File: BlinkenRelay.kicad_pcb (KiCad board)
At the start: 2 copper layers, 90 x 62 mm, 23 parts, among them J1 Conn_02x07_Odd_Even, J2 Conn_01x08_Pin, J3 Conn_01x08_Socket, SW1 SW_DIP_x01, U1 LTV-817, U2 LTV-817, U3 LTV-817, U4 LTV-817, U5 LTV-817, U6 LTV-817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

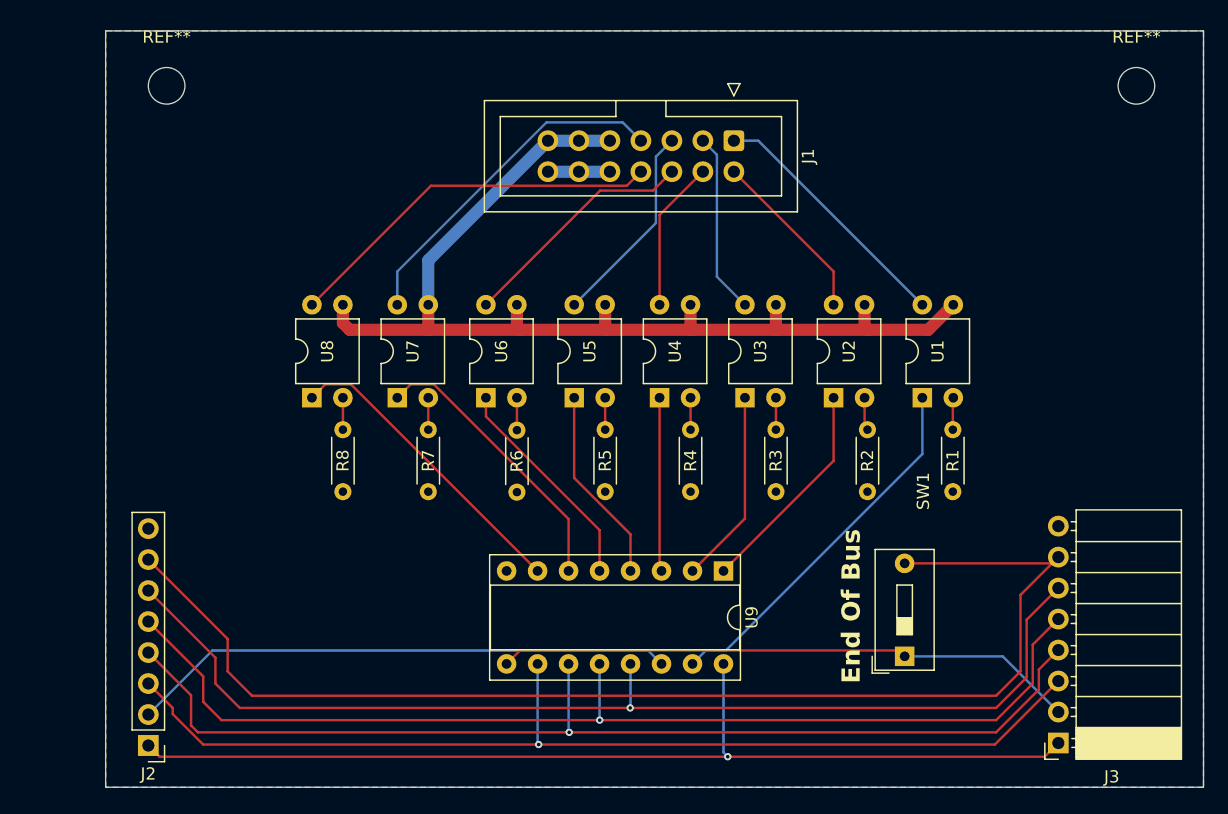
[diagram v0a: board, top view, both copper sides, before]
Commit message: New revision. Fixed switched Pins.
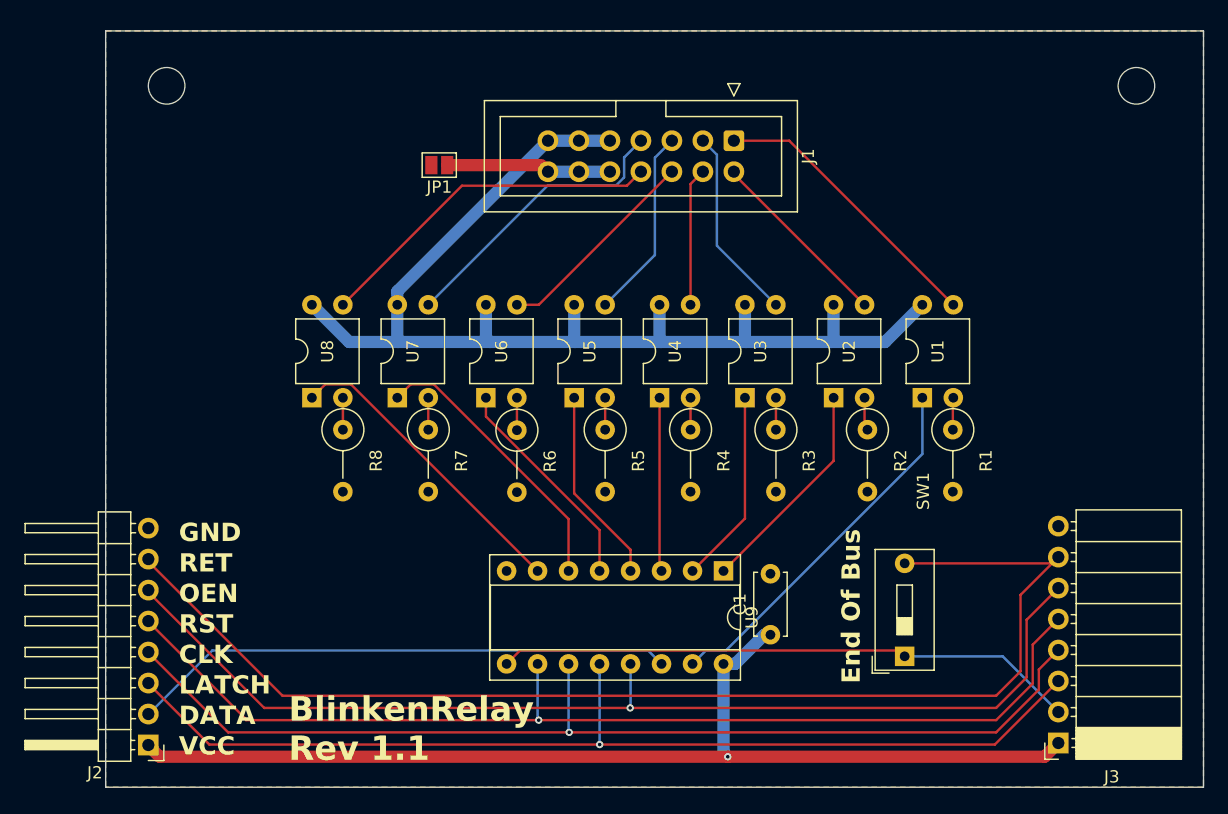
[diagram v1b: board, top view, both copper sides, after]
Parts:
- added C1: 10n, Capacitor_THT:C_Disc_D5.0mm_W2.5mm_P5.00mm, F.Cu at (148.5, 74.5)
- added JP1: Jumper_2_Open, Jumper:SolderJumper-2_P1.3mm_Open_Pad1.0x1.5mm, F.Cu at (121.3, 36.0)
- J2: footprint Connector_PinHeader_2.54mm:PinHeader_1x08_P2.54mm_Vertical -> Connector_PinHeader_2.54mm:PinHeader_1x08_P2.54mm_Horizontal
- R1, R2, R3, R4, R5, R6, R7, R8: value 180 -> 510; footprint Resistor_THT:R_Axial_DIN0204_L3.6mm_D1.6mm_P5.08mm_Horizontal -> Resistor_THT:R_Axial_DIN0309_L9.0mm_D3.2mm_P5.08mm_Vertical
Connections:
- U1 pad 3: +24V -> Kanal 1
- U1 pad 4: Kanal 1 -> +24V
- U2 pad 3: +24V -> Kanal 2
- U2 pad 4: Kanal 2 -> +24V
- U3 pad 3: +24V -> Kanal 3
- U3 pad 4: Kanal 3 -> +24V
- U4 pad 3: +24V -> Kanal 4
- U4 pad 4: Kanal 4 -> +24V
- U5 pad 3: +24V -> Kanal 5
- U5 pad 4: Kanal 5 -> +24V
- U6 pad 3: +24V -> Kanal 6
- U6 pad 4: Kanal 6 -> +24V
- U7 pad 3: +24V -> Kanal 7
- U7 pad 4: Kanal 7 -> +24V
- U8 pad 3: +24V -> Kanal 8
- U8 pad 4: Kanal 8 -> +24V
- U9 pad 10: Strobe -> Reset
- U9 pad 12: Reset -> Strobe
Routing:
- net Net-(J1-Pin_10): track 5.08 -> 13.6 mm
- net +24V: track 87.8 -> 94.9 mm
- net VCC: track 83.2 -> 88.0 mm
- net Kanal 7: track 28.4 -> 24.0 mm
- net Kanal 6: track 19.8 -> 17.2 mm
- net Kanal 1: track 21.0 -> 23.6 mm
- net Kanal 8: track 31.5 -> 28.9 mm
- net Return: track 102.0 -> 99.6 mm
- net Clock: track 88.1 -> 86.7 mm
- net Output Enable: track 90.3 -> 89.0 mm
- net Reset: track 89.1 -> 87.9 mm
- net Kanal 3: track 14.9 -> 15.9 mm
- net Kanal 5: track 16.8 -> 15.7 mm
- net Kanal 4: track 12.4 -> 11.3 mm
- net Kanal 2: track 14.3 -> 15.2 mm
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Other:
- board text added: "BlinkenRelay Rev 1.1"
- board text added: "CLK"
- board text added: "DATA"
- board text added: "GND"
- board text added: "LATCH"
- board text added: "OEN"
- board text added: "RET"
- board text added: "RST"
- board text added: "VCC"

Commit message: Added status LEDS and removed backups from git.
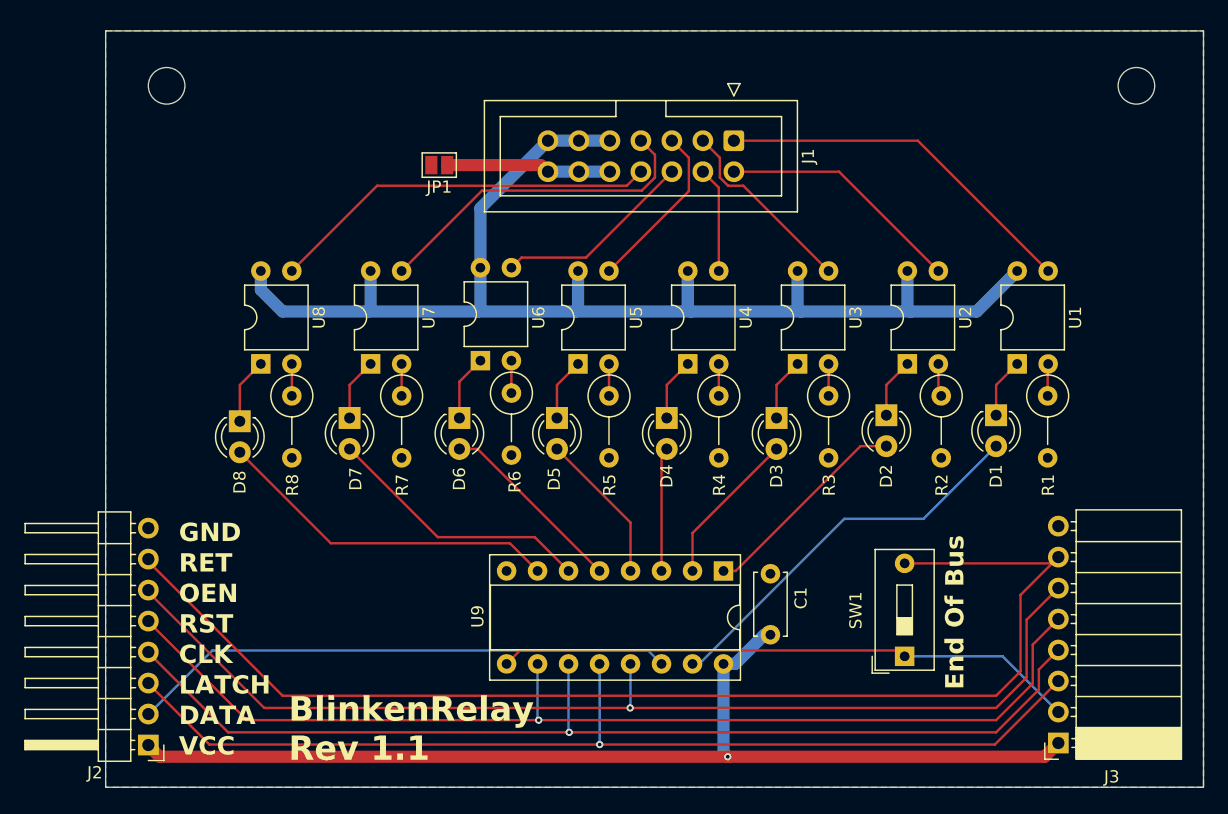
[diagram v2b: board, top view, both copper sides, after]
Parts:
- added D1: LED, LED_THT:LED_D3.0mm, F.Cu at (167.0, 56.5)
- added D2: LED, LED_THT:LED_D3.0mm, F.Cu at (158.0, 56.5)
- added D3: LED, LED_THT:LED_D3.0mm, F.Cu at (149.0, 56.7)
- added D4: LED, LED_THT:LED_D3.0mm, F.Cu at (140.0, 56.7)
- added D5: LED, LED_THT:LED_D3.0mm, F.Cu at (131.0, 56.7)
- added D6: LED, LED_THT:LED_D3.0mm, F.Cu at (123.0, 56.7)
- added D7: LED, LED_THT:LED_D3.0mm, F.Cu at (114.0, 56.7)
- added D8: LED, LED_THT:LED_D3.0mm, F.Cu at (105.0, 57.0)
- R1, R2, R3, R4, R5, R6, R7, R8: value 510 -> 140
- moved U1 8.25 mm to (168.7, 52.3)
- moved R1 8.25 mm to (171.2, 54.9)
- moved R2 6.65 mm to (162.5, 54.9)
- moved U2 6.65 mm to (159.7, 52.3)
- moved U3 5.13 mm to (150.7, 52.3)
- moved R3 5.13 mm to (153.3, 54.9)
- moved U8 5.02 mm to (106.7, 52.3)
- moved R8 5.02 mm to (109.3, 54.9)
- moved U4 3.61 mm to (141.7, 52.3)
- moved R4 3.61 mm to (144.3, 54.9)
- moved U7 3.53 mm to (115.7, 52.3)
- moved R7 3.53 mm to (118.3, 54.9)
- moved R6 3.07 mm to (127.3, 54.7)
- moved U6 3.07 mm to (124.7, 52.0)
- moved U5 2.79 mm to (132.7, 52.3)
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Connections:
- U1 pad 1: Net-(U9-QA) -> Net-(D1-K)
- U2 pad 1: Net-(U9-QB) -> Net-(D2-K)
- U3 pad 1: Net-(U9-QC) -> Net-(D3-K)
- U4 pad 1: Net-(U9-QD) -> Net-(D4-K)
- U5 pad 1: Net-(U9-QE) -> Net-(D5-K)
- U6 pad 1: Net-(U9-QF) -> Net-(D6-K)
- U7 pad 1: Net-(U9-QG) -> Net-(D7-K)
- U8 pad 1: Net-(U9-QH) -> Net-(D8-K)
- U9 pad 1: Net-(U9-QB) -> Net-(D2-A)
- U9 pad 15: Net-(U9-QA) -> Net-(D1-A)
- U9 pad 2: Net-(U9-QC) -> Net-(D3-A)
- U9 pad 3: Net-(U9-QD) -> Net-(D4-A)
- U9 pad 4: Net-(U9-QE) -> Net-(D5-A)
- U9 pad 5: Net-(U9-QF) -> Net-(D6-A)
- U9 pad 6: Net-(U9-QG) -> Net-(D7-A)
- U9 pad 7: Net-(U9-QH) -> Net-(D8-A)
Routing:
- net Net-(D1-A): track 0.00 -> 32.3 mm
- net Net-(U9-QA): track 30.6 -> 0.00 mm
- net Net-(D8-A): track 0.00 -> 28.4 mm
- net Net-(U9-QH): track 25.3 -> 0.00 mm
- net Net-(U9-QG): track 23.3 -> 0.00 mm
- net Net-(D7-A): track 0.00 -> 22.1 mm
- net Net-(U9-QF): track 18.1 -> 0.00 mm
- net Net-(U9-QB): track 17.9 -> 0.00 mm
- net Net-(D2-A): track 0.00 -> 17.6 mm
- net Net-(U9-QE): track 16.1 -> 0.00 mm
- net Net-(U9-QC): track 16.0 -> 0.00 mm
- net Net-(D6-A): track 0.00 -> 15.6 mm
- net Net-(U9-QD): track 14.0 -> 0.00 mm
- net Net-(D3-A): track 0.00 -> 12.9 mm
- net Net-(D5-A): track 0.00 -> 12.5 mm
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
